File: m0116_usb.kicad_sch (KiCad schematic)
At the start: 182 parts, among them J1 AVR-ISP-6, J2 Conn_01x04, J3 Conn_01x04, U1 ATmega32A-PU

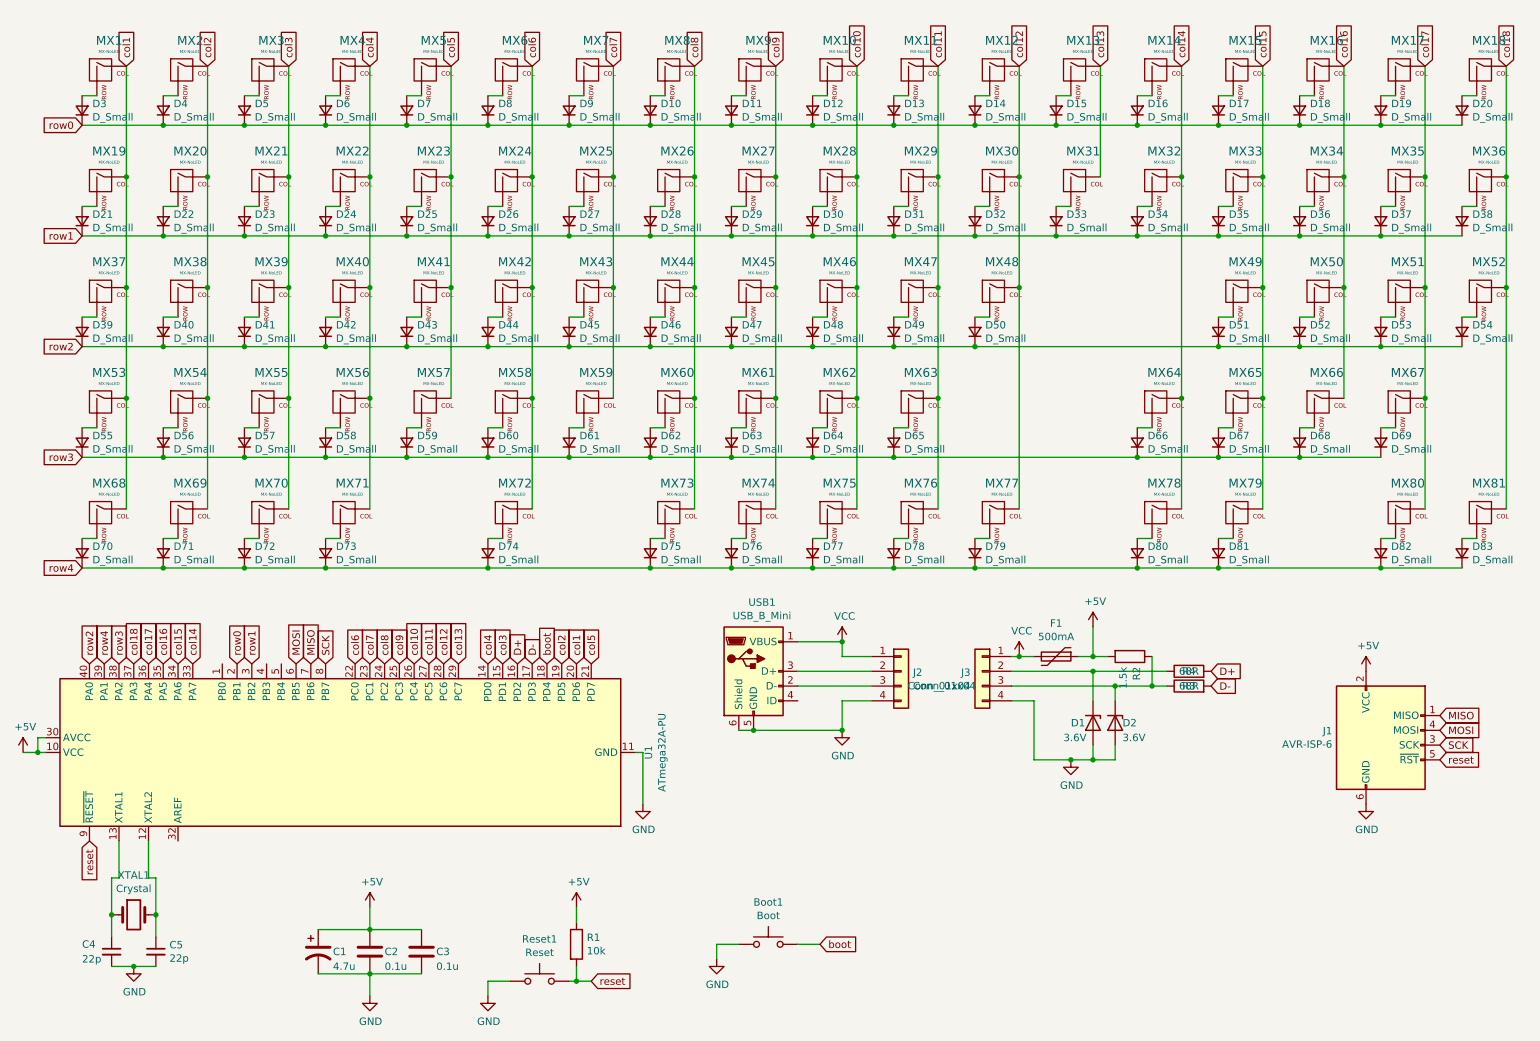
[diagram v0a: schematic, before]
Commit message: Replace ATmega/V-USB controller with nice!nano v2 schematic
Schematic-only change for Revision A of the wireless TrackPoint mod.
The PCB has not been updated yet.

Root sheet: the 5x18 matrix (81 switches, 81 diodes) is unchanged and
now connects to a new "Controller" sub-sheet through the existing
global labels row0-row4 / col1-col18. Removed the ATmega32A, V-USB
circuit, crystal, ISP header, mini-USB, polyfuse and boot button.

controller.kicad_sch:
- nice!nano v2 (socketed, Pro Micro footprint) with reset button;
  rows on native GPIOs for key-press wake-up
- 3x 74HC595 daisy-chained over SPI drive col1-col18, 100n each
- LiPo (JST PH) -> slide switch -> B+
- MCP1700 always-on LDO for the shift registers, because ZMK turns
  the nice!nano VCC pin off in deep sleep; JP1 selects LDO or VCC
- TrackPoint powered from nice!nano switched VCC, 4k7 PS/2 pull-ups,
  100k reset pull-down, generic 1x10 adapter header
- test pads for battery, rails, TrackPoint supply and PS/2

New project symbol library m0116_wireless (nice!nano v2); the
rescue library from the KiCad 7 conversion is no longer needed.

ERC: 0 errors, 0 warnings. Matrix connectivity verified identical to
the original netlist.

Co-Authored-By: Claude Opus 5.5 <noreply@anthropic.com>
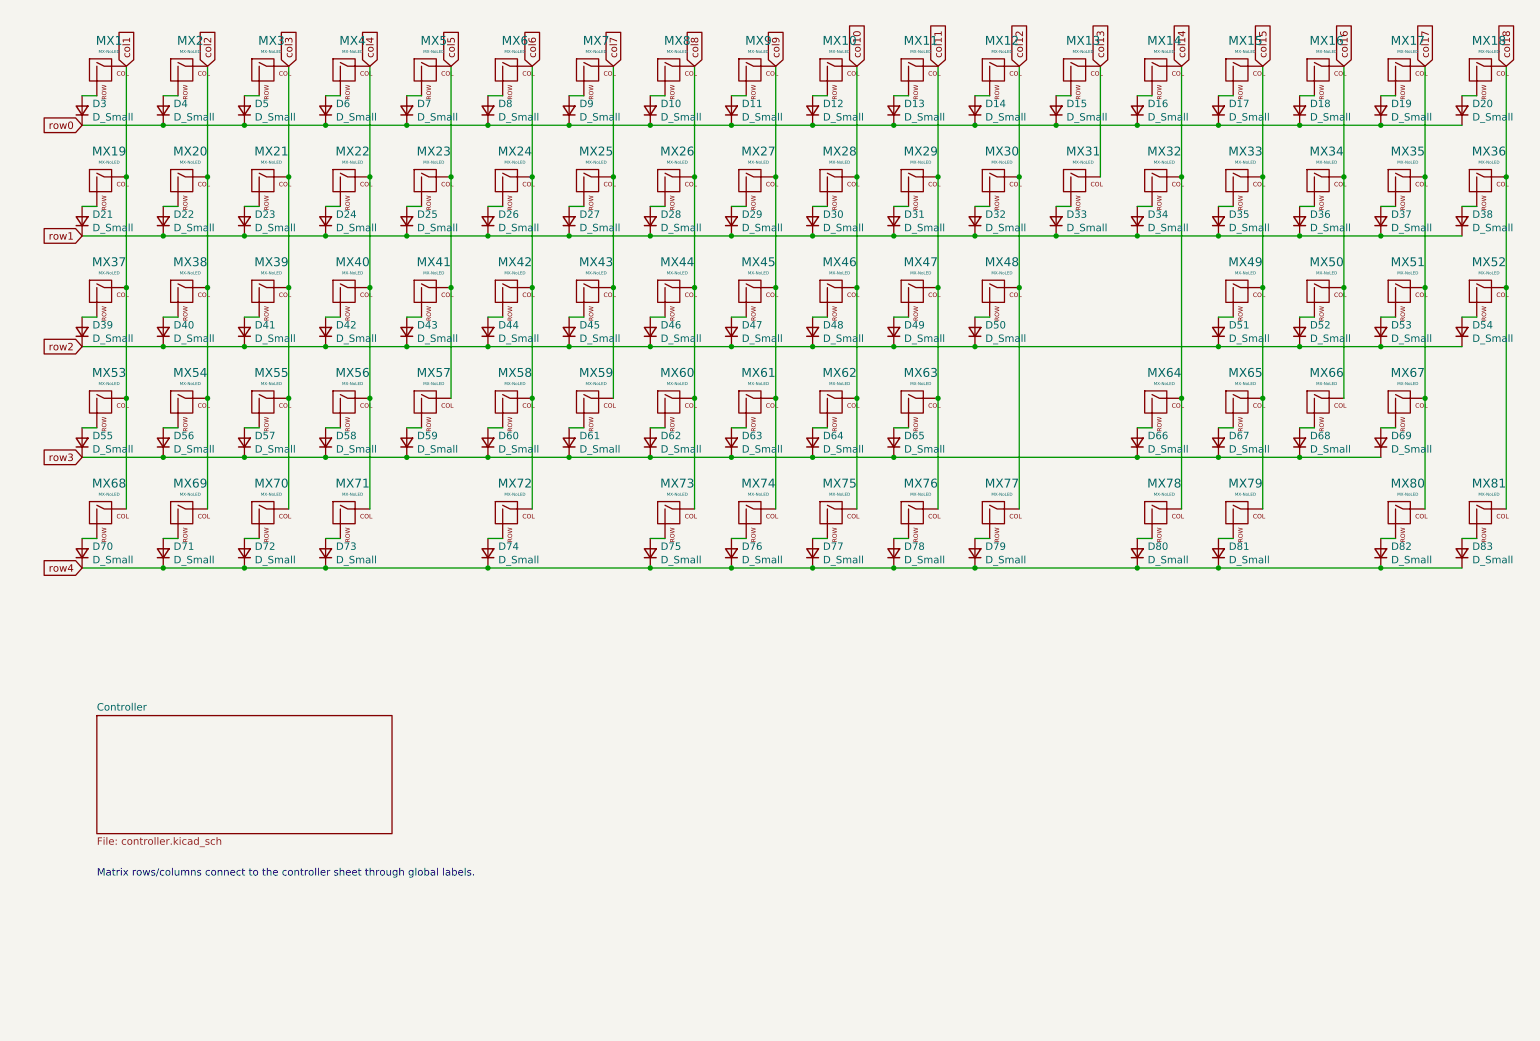
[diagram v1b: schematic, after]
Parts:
- removed Boot1: Boot, Button_Switch_THT:SW_PUSH_6mm, symbol Switch:SW_Push
- removed C1: 4.7u, Capacitor_THT:CP_Radial_D5.0mm_P2.50mm, symbol m0116_usb-rescue:CP1-Device
- removed C2, C3: 0.1u, Capacitor_THT:C_Disc_D3.0mm_W2.0mm_P2.50mm, symbol Device:C
- removed C4, C5: 22p, Capacitor_THT:C_Disc_D6.0mm_W2.5mm_P5.00mm, symbol Device:C_Small
- removed D1, D2: 3.6V, Diode_THT:D_DO-35_SOD27_P7.62mm_Horizontal, symbol Device:D_Zener
- removed F1: 500mA, Fuse:Fuse_Littelfuse_395Series, symbol Device:Polyfuse
- removed J1: AVR-ISP-6, Connector_PinHeader_2.54mm:PinHeader_2x03_P2.54mm_Horizontal, symbol Connector:AVR-ISP-6
- removed J2: Conn_01x04, Connector_PinHeader_2.00mm:PinHeader_1x04_P2.00mm_Vertical, symbol Connector_Generic:Conn_01x04
- removed J3: Conn_01x04, Connector_JST:JST_PH_S4B-PH-K_1x04_P2.00mm_Horizontal, symbol Connector_Generic:Conn_01x04
- removed R1: 10k, Resistor_THT:R_Axial_DIN0207_L6.3mm_D2.5mm_P10.16mm_Horizontal, symbol Device:R
- removed R2: 1.5k, Resistor_THT:R_Axial_DIN0207_L6.3mm_D2.5mm_P10.16mm_Horizontal, symbol Device:R
- removed R3, R4: 68R, Resistor_THT:R_Axial_DIN0207_L6.3mm_D2.5mm_P10.16mm_Horizontal, symbol Device:R
- removed Reset1: Reset, Button_Switch_THT:SW_PUSH_6mm, symbol Switch:SW_Push
- removed U1: ATmega32A-PU, Package_DIP:DIP-40_W15.24mm_Socket, symbol m0116_usb-rescue:ATmega32A-PU-MCU_Microchip_ATmega
- removed USB1: USB_B_Mini, random-keyboard-parts:Molex-0548190519, symbol m0116_usb-rescue:USB_B_Mini-Connector
- removed XTAL1: Crystal, Crystal:Crystal_HC49-4H_Vertical, symbol Device:Crystal
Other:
- added sheet Controller (controller.kicad_sch)
- note added: "Matrix rows/columns connect to the controller sheet through global labels."

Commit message: Add USB-C pass-through daughterboard schematic
The nice!nano USB-C port is not reachable from outside the case. Keep
the original break-off daughterboard concept (tab glued into the rear
ADB cut-out) and turn it into a USB-C pass-through:

- J3: GCT USB4085 THT USB-C receptacle facing outward, 5.1k Rd on
  CC1/CC2 (R4/R5) so USB-C hosts and chargers supply VBUS
- J4: second USB4085 facing inward; a short off-the-shelf USB 2.0
  C-to-C cable connects it to the nice!nano (CC left open, the
  nice!nano has its own Rd)
- DB_* nets live only on the tab, so breaking it off leaves no
  unrouted connections to the main board

ERC: 0 errors, 0 warnings.

Co-Authored-By: Claude Opus 5.5 <noreply@anthropic.com>
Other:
- added sheet USB daughterboard (usb_daughterboard.kicad_sch)
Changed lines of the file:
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@@
+    )
+  )
+  (sheet (at 91.44 134.62) (size 50.8 20.32) (fields_autoplaced)
+    (stroke (width 0.1524) (type solid))
+    (fill (color 0 0 0 0.0000))
+    (property "Sheetname" "USB daughterboard" (at 91.44 133.9086 0)
+      (effects (font (size 1.27 1.27)) (justify left bottom))
+    )
+    (property "Sheetfile" "usb_daughterboard.kicad_sch" (at 91.44 155.5246 0)
+      (effects (font (size 1.27 1.27)) (justify left top))
+    )
+    (instances
+      (project "m0116_usb"
+        (path "/bd040ff9-43ec-4b84-8454-d4faf6313801" (page "3"))
+      )
     )
   )

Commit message: Add MX/Alps hybrid footprints, TKL variant and Freerouting workflow
Snapshot, routing still in progress.

- switch footprints changed to MX_Alps_Hybrid:MX-1U-NoLED, optional
  centred MX spacebar switch MX82
- m0116_tkl: board without keypad, generated by make tkl-sch / tkl-pcb,
  right edge copies the original contour; partially autorouted
  (open: col2, GND islands near U2/U3, USB daughterboard by hand)
- tools/export_matrix_dsn.py, tools/import_ses.py: Specctra DSN/SES
  round trip for Freerouting (make dsn, make dsn-continue)
- full board: old matrix tracks still cross the MX centre holes until
  it is rerouted

Co-Authored-By: Claude Opus 5.5 <noreply@anthropic.com>
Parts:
- added MX82: MX-NoLED, MX_Alps_Hybrid:MX-1U-NoLED, symbol MX_Alps_Hybrid:MX-NoLED
- MX1, MX10, MX11, MX12, MX13, MX14, MX15, MX16, MX17, MX18, MX19, MX2, MX20, MX21, MX22, MX23, MX24, MX25, MX26, MX27, MX28, MX29, MX3, MX30, MX31, MX32, MX33, MX34, MX35, MX36, MX37, MX38, MX39, MX4, MX40, MX41, MX42, MX43, MX44, MX45, MX46, MX47, MX48, MX49, MX5, MX50, MX51, MX52, MX53, MX54, MX55, MX56, MX57, MX58, MX59, MX6, MX60, MX61, MX62, MX63, MX64, MX65, MX66, MX67, MX68, MX69, MX7, MX70, MX71, MX72, MX73, MX74, MX75, MX76, MX77, MX78, MX79, MX8, MX80, MX81, MX9: footprint Alps_Only:ALPS-1U -> MX_Alps_Hybrid:MX-1U-NoLED
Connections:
- net col8: now also MX82.1 (COL)
- net SPACE_SW: now reaches D75.2 (A), MX73.2 (ROW)
- net SPACE_SW: now also MX82.2 (ROW)
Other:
- note added: "MX82: alternative spacebar switch at the keycap centre for MX spacebars, in parallel with MX73 (off-centre, original Alps position). Populate only one."
